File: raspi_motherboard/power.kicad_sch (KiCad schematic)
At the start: 30 parts, among them J3 Conn_01x03, U3 TPS563200

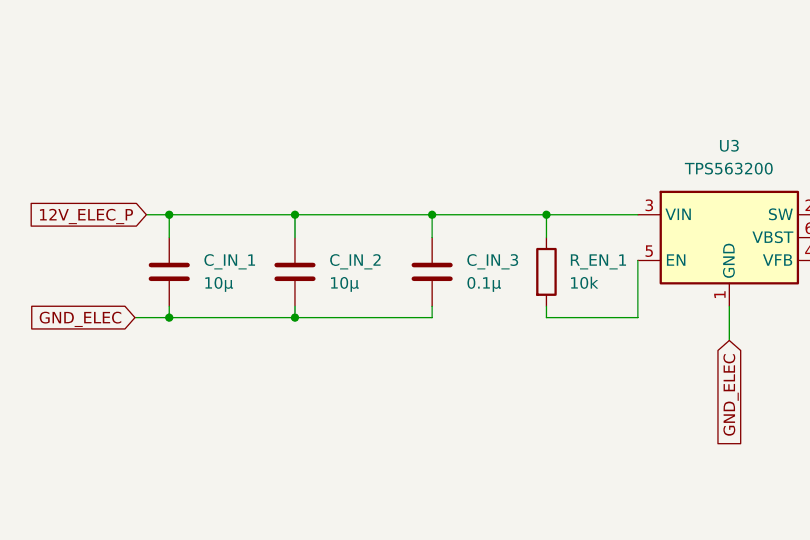
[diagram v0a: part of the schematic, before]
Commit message: [WiP] start putting refs in silkscreen
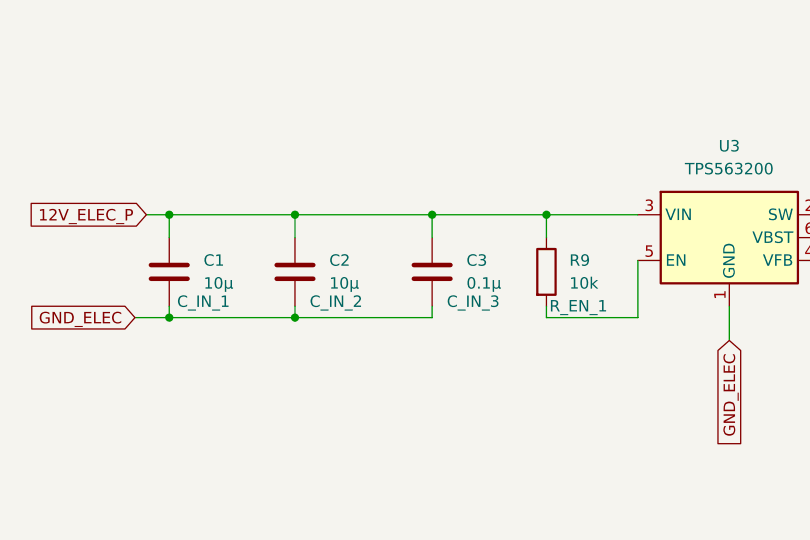
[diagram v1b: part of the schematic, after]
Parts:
- renumbered C_IN_1 to C1, C_IN_2 to C2, C_IN_3 to C3, R_EN_1 to R9
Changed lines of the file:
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@@
 		(on_board yes)
 		(dnp no)
-		(fields_autoplaced yes)
-		(property "Reference" "C_IN_2"
+		(property "Reference" "C2"
 			(at 170.18 93.98 0)
 			(effects
@@
 			)
 		)
-		(property "Description" ""
-			(at 166.37 95.25 0)
-			(effects
-				(font
-					(size 1.27 1.27)
-				)
-				(hide yes)
-			)
-		)
-		(pin "1"
-		)
-		(pin "2"
-		)
-		(instances
-			(project "power_motherboard"
-				(path "/e63e39d7-6ac0-4ffd-8aa3-1841a4541b55/4c6639a9-406a-464b-9012-e90cb018ad22"
-					(reference "C_IN_2")
+		(property "Description" "C_IN_2"
+			(at 170.942 98.552 0)
+			(effects
+				(font
+					(size 1.27 1.27)
+				)
+			)
+		)
+		(pin "1"
+		)
+		(pin "2"
+		)
+		(instances
+			(project "power_motherboard"
+				(path "/e63e39d7-6ac0-4ffd-8aa3-1841a4541b55/4c6639a9-406a-464b-9012-e90cb018ad22"
+					(reference "C2")
 					(unit 1)
 				)
@@
 		(on_board yes)
 		(dnp no)
-		(fields_autoplaced yes)
-		(property "Reference" "C_IN_3"
+		(property "Reference" "C3"
 			(at 185.42 93.98 0)
 			(effects
@@
 			)
 		)
-		(property "Description" ""
-			(at 181.61 95.25 0)
-			(effects
-				(font
-					(size 1.27 1.27)
-				)
-				(hide yes)
-			)
-		)
-		(pin "1"
-		)
-		(pin "2"
-		)
-		(instances
-			(project "power_motherboard"
-				(path "/e63e39d7-6ac0-4ffd-8aa3-1841a4541b55/4c6639a9-406a-464b-9012-e90cb018ad22"
-					(reference "C_IN_3")
+		(property "Description" "C_IN_3"
+			(at 186.182 98.552 0)
+			(effects
+				(font
+					(size 1.27 1.27)
+				)
+			)
+		)
+		(pin "1"
+		)
+		(pin "2"
+		)
+		(instances
+			(project "power_motherboard"
+				(path "/e63e39d7-6ac0-4ffd-8aa3-1841a4541b55/4c6639a9-406a-464b-9012-e90cb018ad22"
+					(reference "C3")
 					(unit 1)
 				)
@@
 		(on_board yes)
 		(dnp no)
-		(fields_autoplaced yes)
-		(property "Reference" "R_EN_1"
+		(property "Reference" "R9"
 			(at 196.85 93.98 0)
 			(effects
@@
 			)
 		)
-		(property "Description" ""
-			(at 194.31 95.25 0)
-			(effects
-				(font
-					(size 1.27 1.27)
-				)
-				(hide yes)
-			)
-		)
-		(pin "1"
-		)
-		(pin "2"
-		)
-		(instances
-			(project "power_motherboard"
-				(path "/e63e39d7-6ac0-4ffd-8aa3-1841a4541b55/4c6639a9-406a-464b-9012-e90cb018ad22"
-					(reference "R_EN_1")
+		(property "Description" "R_EN_1"
+			(at 197.866 99.06 0)
+			(effects
+				(font
+					(size 1.27 1.27)
+				)
+			)
+		)
+		(pin "1"
+		)
+		(pin "2"
+		)
+		(instances
+			(project "power_motherboard"
+				(path "/e63e39d7-6ac0-4ffd-8aa3-1841a4541b55/4c6639a9-406a-464b-9012-e90cb018ad22"
+					(reference "R9")
 					(unit 1)
 				)
@@
 		(on_board yes)
 		(dnp no)
-		(fields_autoplaced yes)
-		(property "Reference" "C_IN_1"
+		(property "Reference" "C1"
 			(at 156.21 93.98 0)
 			(effects
@@
 			)
 		)
-		(property "Description" ""
-			(at 152.4 95.25 0)
-			(effects
-				(font
-					(size 1.27 1.27)
-				)
-				(hide yes)
-			)
-		)
-		(pin "1"
-		)
-		(pin "2"
-		)
-		(instances
-			(project "power_motherboard"
-				(path "/e63e39d7-6ac0-4ffd-8aa3-1841a4541b55/4c6639a9-406a-464b-9012-e90cb018ad22"
-					(reference "C_IN_1")
-					(unit 1)
-				)
+		(property "Description" "C_IN_1"
+			(at 156.21 98.552 0)
+			(effects
+				(font
+					(size 1.27 1.27)
+				)
+			)
+		)
+		(pin "1"
+		)
+		(pin "2"
+		)
+		(instances
+			(project "power_motherboard"
+				(path "/e63e39d7-6ac0-4ffd-8aa3-1841a4541b55/4c6639a9-406a-464b-9012-e90cb018ad22"
+					(reference "C1")
+					(unit 1)
+				)
